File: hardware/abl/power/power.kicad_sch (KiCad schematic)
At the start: 34 parts, among them J1 Terminal_01x03, J2 Terminal_01x03, J3 009159008603906, U1 TWGMC AMS1117-3.3, U2 TMP1075D, U3 INA219AxD, U4 24AA025UIDT-I/OT

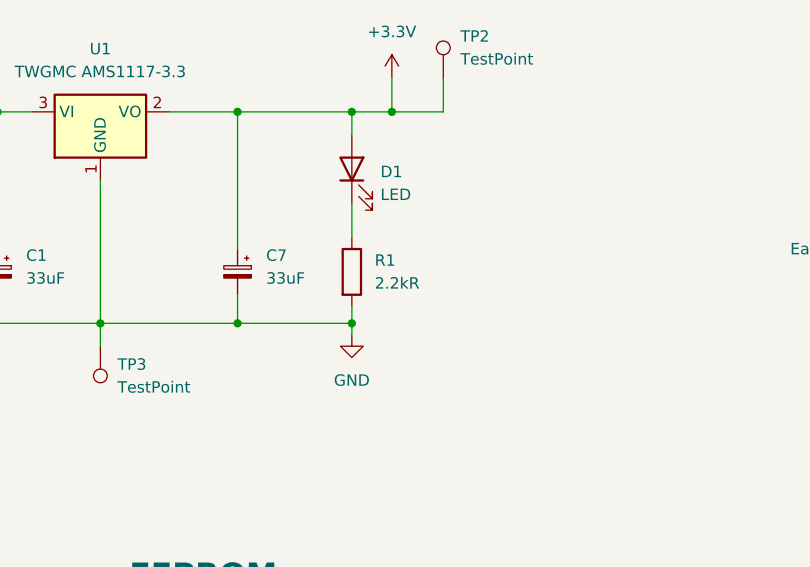
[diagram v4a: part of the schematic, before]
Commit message: Move LED and let it shine brighter, extend outline, many small enhancements.
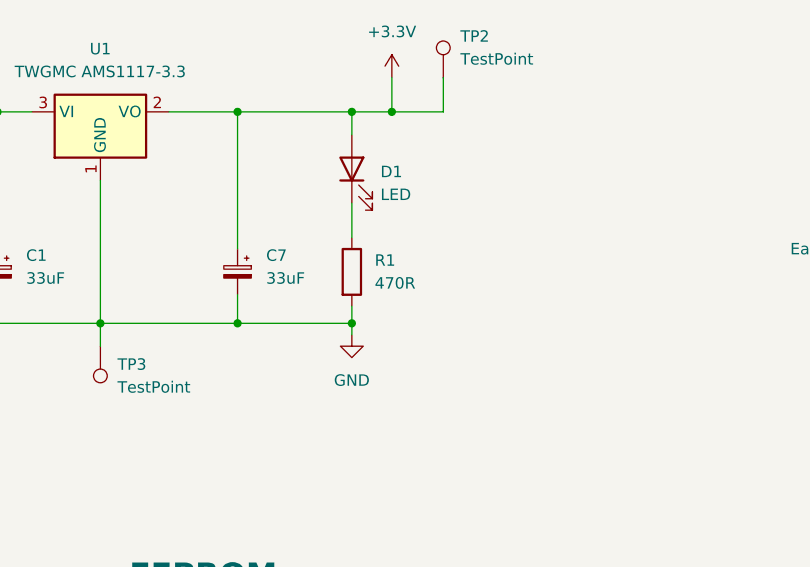
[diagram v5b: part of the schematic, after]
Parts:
- JP1: footprint Jumper:SolderJumper-3_P1.3mm_Open_RoundedPad1.0x1.5mm -> Jumper:SolderJumper-3_P1.3mm_Bridged12_RoundedPad1.0x1.5mm
- R1: value 2.2kR -> 470R; footprint Resistor_SMD:R_0402_1005Metric -> Resistor_SMD:R_0603_1608Metric; LCSC Part C25879 -> C23179; Manufacturer_Part_Number 0402WGF2201TCE -> 0603WAF4700T5E
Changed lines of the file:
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@@
 	(title_block
 		(title "besteLampe! ABL Power Module")
-		(date "2024-11-01")
-		(rev "1.1")
-		(comment 1 "See  https://lenaschimmel.de/besteLampe! for the source and more information")
+		(date "2024-11-10")
+		(rev "1.2")
+		(comment 1 "See https://beste-lampe.de for the source and more information")
 		(comment 2 "This source describes Open Hardware and is licensed under the CERN-OHL-S v2.")
 		(comment 3 "Copyright 2024 Lena Schimmel <mail@lenaschimmel.de>")
@@
 			)
 		)
-		(property "Value" "2.2kR"
+		(property "Value" "470R"
 			(at 76.835 63.4999 0)
 			(effects
@@
 			)
 		)
-		(property "Footprint" "Resistor_SMD:R_0402_1005Metric"
+		(property "Footprint" "Resistor_SMD:R_0603_1608Metric"
 			(at 72.517 62.23 90)
 			(effects
@@
 			)
 		)
-		(property "LCSC Part" "C25879"
+		(property "LCSC Part" "C23179"
 			(at 74.295 62.23 0)
 			(effects
@@
 			)
 		)
-		(property "Manufacturer_Part_Number" "0402WGF2201TCE"
+		(property "Manufacturer_Part_Number" "0603WAF4700T5E"
 			(at 74.295 62.23 0)
 			(effects
@@
 			)
 		)
-		(property "Footprint" "Jumper:SolderJumper-3_P1.3mm_Open_RoundedPad1.0x1.5mm"
+		(property "Footprint" "Jumper:SolderJumper-3_P1.3mm_Bridged12_RoundedPad1.0x1.5mm"
 			(at 259.08 131.445 0)
 			(effects

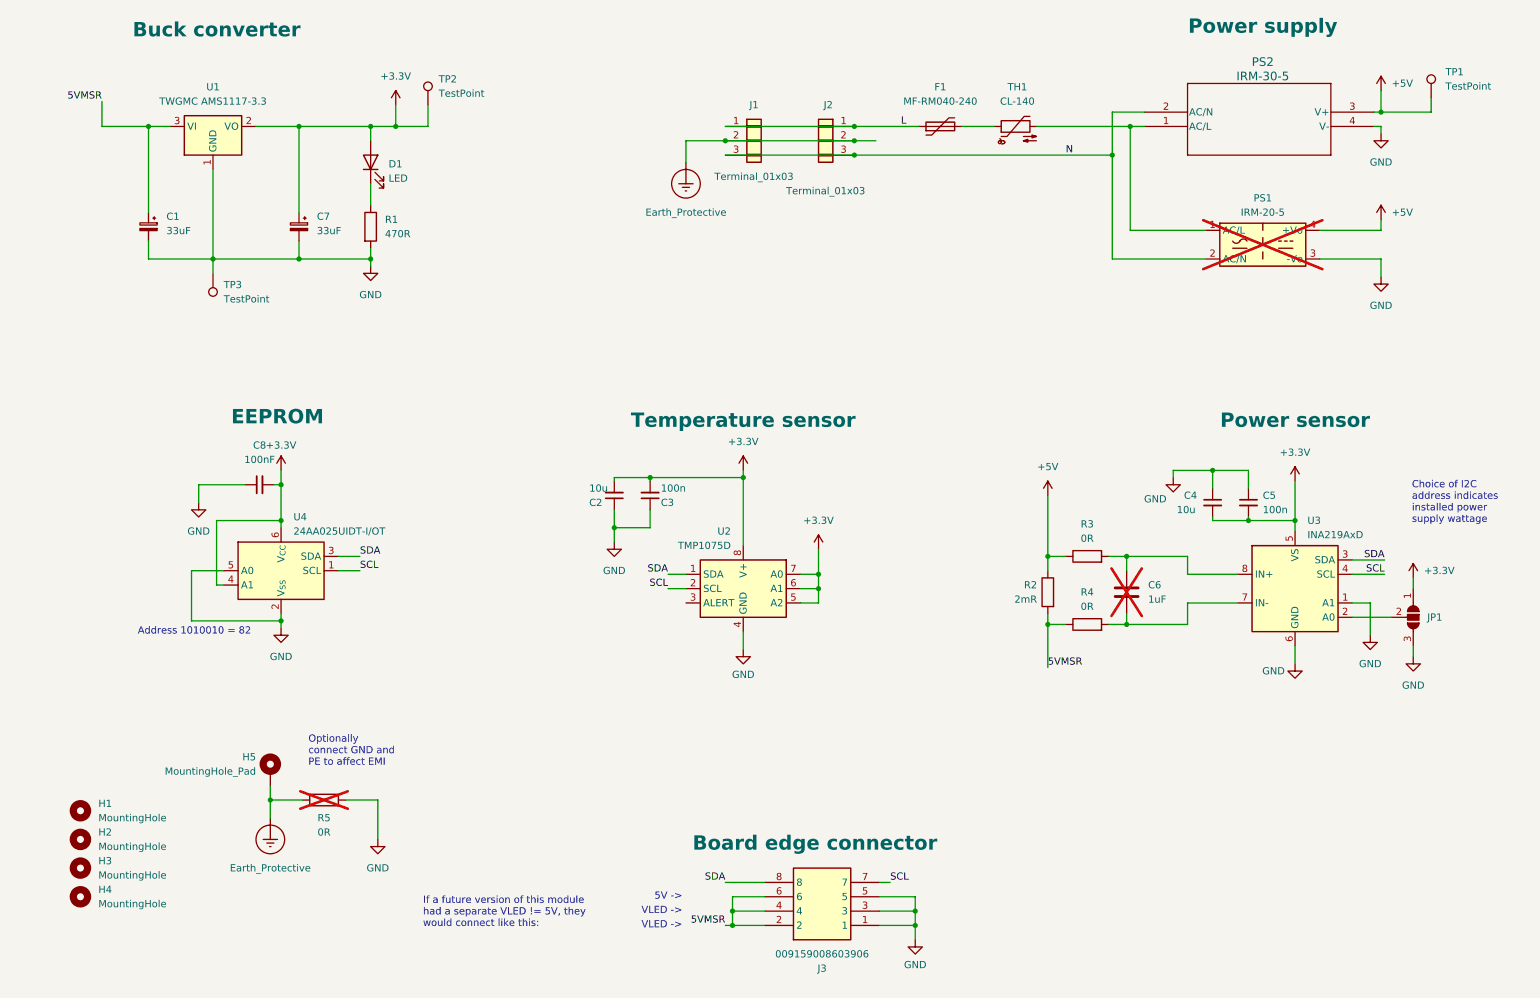
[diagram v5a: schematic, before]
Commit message: Greatly increase clearance for 230V tracks. Chosen 30W power supply and removed option for 20W. Many other small improvements.
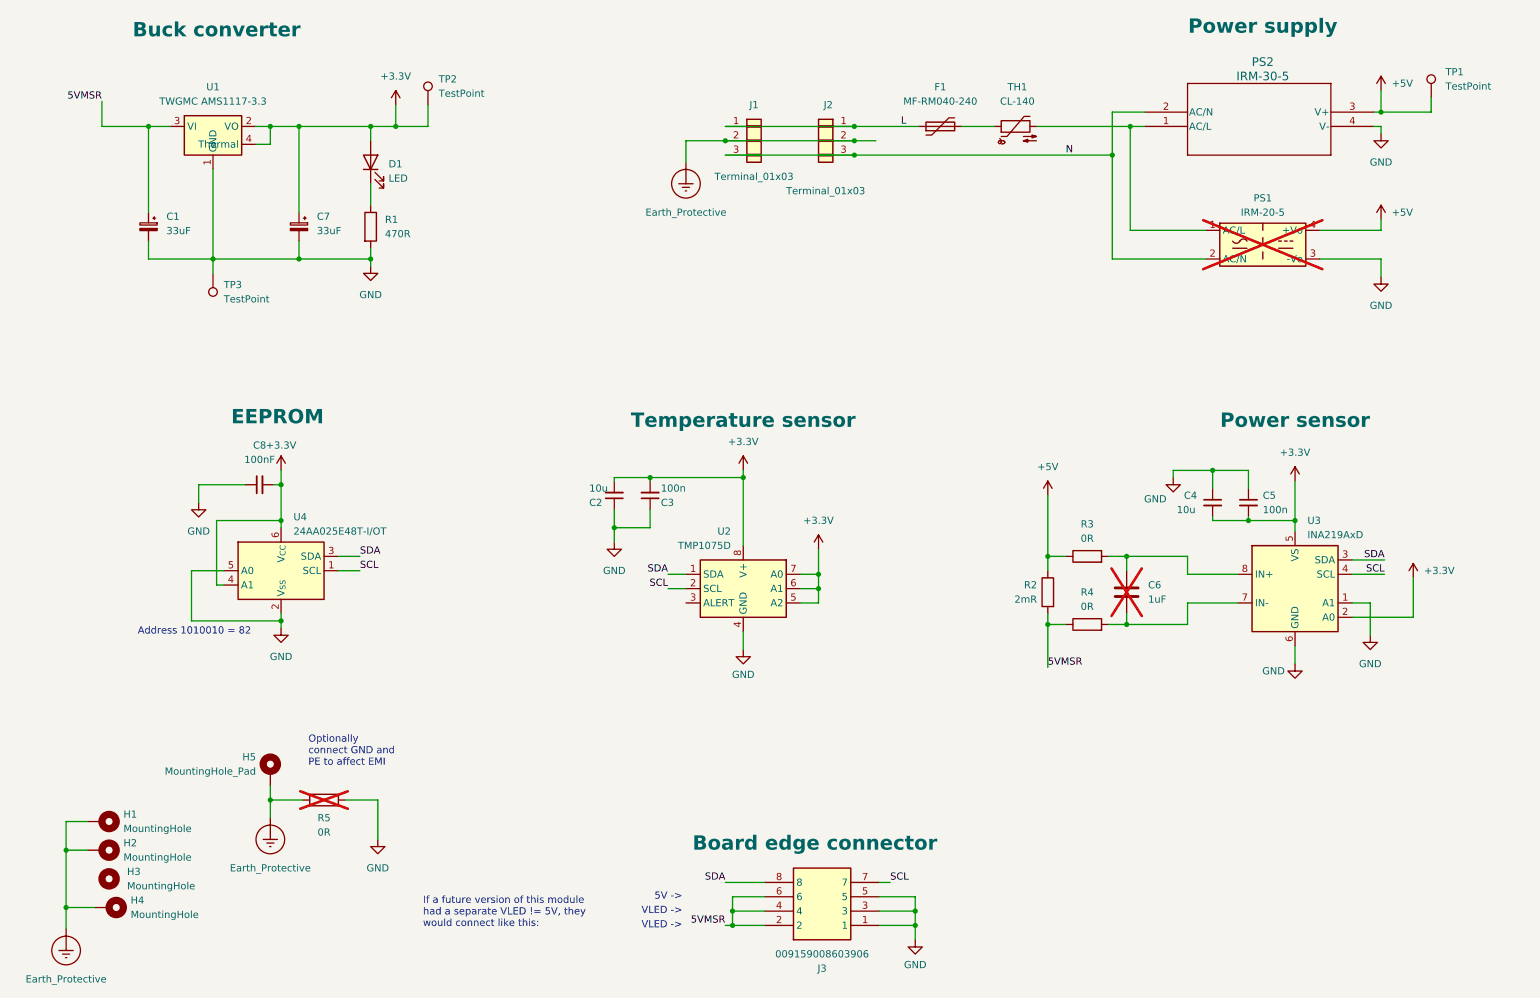
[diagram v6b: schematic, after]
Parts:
- removed JP1: SolderJumper_3_Bridged12, Jumper:SolderJumper-3_P1.3mm_Bridged12_RoundedPad1.0x1.5mm, symbol Jumper:SolderJumper_3_Open
- H1, H2, H4: footprint MountingHole:MountingHole_3.2mm_M3_DIN965 -> MountingHole:MountingHole_3.2mm_M3_DIN965_Pad_TopOnly; symbol Mechanical:MountingHole -> Mechanical:MountingHole_Pad
- PS2: footprint Own footprints:Converter_ACDC_MeanWell_IRM-20+30-xx_THT_combined -> Own footprints:Converter_ACDC_MeanWell_IRM-30-xx_THT
- U1: footprint Package_TO_SOT_SMD:SOT-223 -> Package_TO_SOT_SMD:SOT-223-3_TabPin2; symbol Regulator_Linear:AMS1117-3.3 -> Regulator_Linear:AMS1117-3.3-Thermal-pad
- U4: value 24AA025UIDT-I/OT -> 24AA025E48T-I/OT; LCSC Part (none) -> C2061498; LCSC Part # C2061498 -> C129895; Manufacturer_Part_Number 24AA025UIDT-I/OT -> 24AA025E48T-I/OT
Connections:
- net +3.3V: now also U1.4 (Thermal), U3.2 (A0)
- net Earth_Protective: now also H1.1, H2.1, H4.1
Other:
- moved on the sheet: H3

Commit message: Many small adjustments for the next production run.
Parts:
- C8: value 100nF -> 100n; LCSC Part (none) -> C1525
- F1, H1, H2, H3, H4, H5, J1, J2, PS2, TH1, TP1, TP2, TP3: now not fitted
- J3: LCSC Part (none) -> C22394454
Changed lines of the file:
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@@
 	(title_block
 		(title "besteLampe! ABL Power Module")
-		(date "2024-11-12")
-		(rev "1.2")
+		(date "2024-11-26")
+		(rev "1.2.1")
 		(comment 1 "See https://beste-lampe.de for the source and more information")
 		(comment 2 "This source describes Open Hardware and is licensed under the CERN-OHL-S v2.")
@@
 		(in_bom no)
 		(on_board yes)
-		(dnp no)
+		(dnp yes)
 		(fields_autoplaced yes)
 		(property "Reference" "H3"
@@
 		(in_bom yes)
 		(on_board yes)
-		(dnp no)
+		(dnp yes)
 		(fields_autoplaced yes)
 		(property "Reference" "F1"
@@
 		(in_bom yes)
 		(on_board yes)
-		(dnp no)
+		(dnp yes)
 		(property "Reference" "TP2"
 			(at 86.36 36.0679 0)
@@
 		(in_bom no)
 		(on_board yes)
-		(dnp no)
+		(dnp yes)
 		(property "Reference" "H5"
 			(at 53.975 156.2099 0)
@@
 		(in_bom no)
 		(on_board yes)
-		(dnp no)
+		(dnp yes)
 		(fields_autoplaced yes)
 		(property "Reference" "H4"
@@
 		(in_bom yes)
 		(on_board yes)
-		(dnp no)
+		(dnp yes)
 		(fields_autoplaced yes)
 		(property "Reference" "TP1"
@@
 		(in_bom yes)
 		(on_board yes)
-		(dnp no)
+		(dnp yes)
 		(fields_autoplaced yes)
 		(property "Reference" "TH1"
@@
 		(in_bom yes)
 		(on_board yes)
-		(dnp no)
+		(dnp yes)
 		(property "Reference" "J1"
 			(at 142.24 40.64 0)
@@
 		(in_bom no)
 		(on_board yes)
-		(dnp no)
+		(dnp yes)
 		(fields_autoplaced yes)
 		(property "Reference" "H1"
@@
 		(in_bom yes)
 		(on_board yes)
-		(dnp no)
+		(dnp yes)
 		(property "Reference" "J2"
 			(at 156.21 40.64 0)
@@
 			)
 		)
+		(property "LCSC Part" "C22394454"
+			(at 144.145 186.055 0)
+			(effects
+				(font
+					(size 1.27 1.27)
+				)
+				(hide yes)
+			)
+		)
 		(pin "8"
 		)
@@
 		(in_bom yes)
 		(on_board yes)
-		(dnp no)
+		(dnp yes)
 		(fields_autoplaced yes)
 		(property "Reference" "TP3"
@@
 			)
 		)
-		(property "Value" "100nF"
+		(property "Value" "100n"
 			(at 54.6163 103.505 90)
 			(effects
@@
 			)
 		)
+		(property "LCSC Part" "C1525"
+			(at 54.61 107.95 0)
+			(effects
+				(font
+					(size 1.27 1.27)
+				)
+				(hide yes)
+			)
+		)
 		(pin "1"
 		)
@@
 		(in_bom no)
 		(on_board yes)
-		(dnp no)
+		(dnp yes)
 		(fields_autoplaced yes)
 		(property "Reference" "H2"
@@
 		(in_bom yes)
 		(on_board yes)
-		(dnp no)
+		(dnp yes)
 		(property "Reference" "PS2"
 			(at 232.41 33.02 0)
